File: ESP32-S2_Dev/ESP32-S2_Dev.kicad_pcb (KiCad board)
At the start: 4 copper layers, 47 x 67.3 mm, 114 parts, among them Q1 MMBT3906, Q2 BCW66GLT1G, Q3 BCW66GLT1G, U1 CP2102N-A01-GQFN28, U2 BD00C0AWFPS-ME2, U3 ESP32-S2, Y1 KC2520C40.0000C2YE00, Y2 Crystal

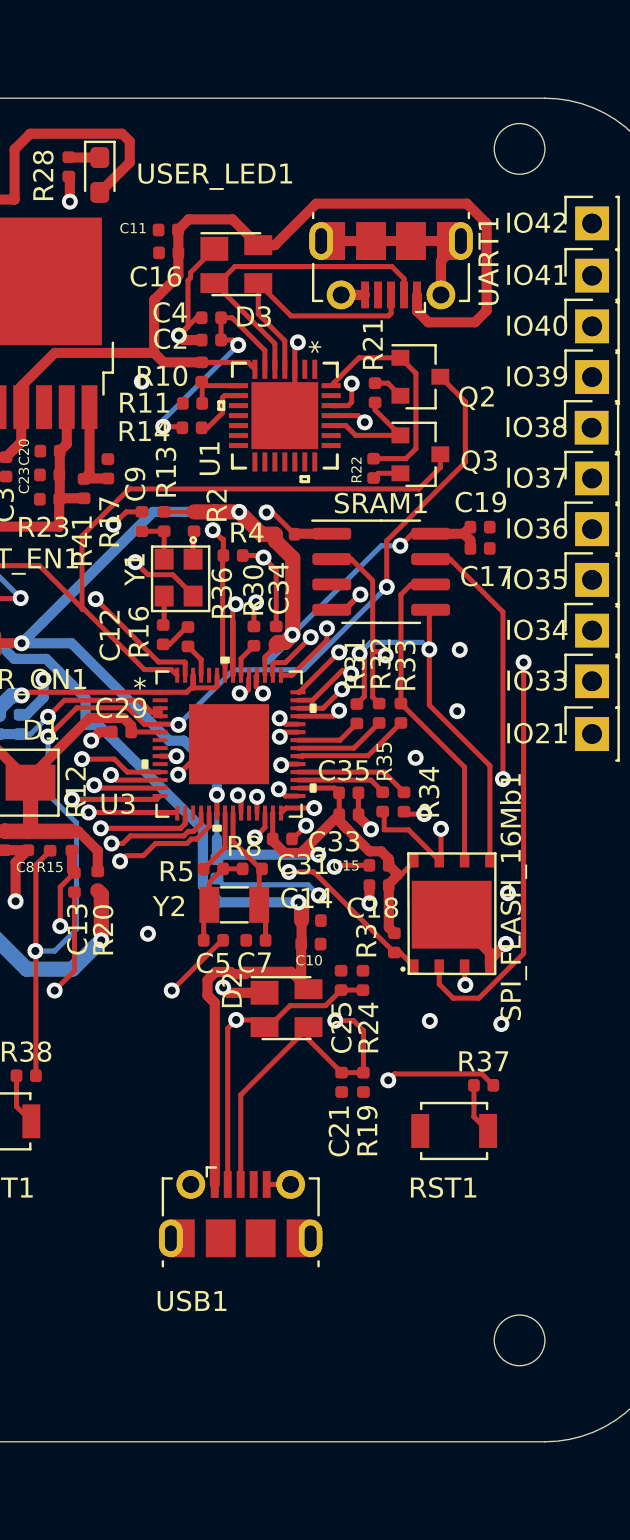
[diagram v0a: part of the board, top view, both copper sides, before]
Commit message: updated layout to move usb connectors closer to the edges, as they are today pluggin in will be nigh impossible.
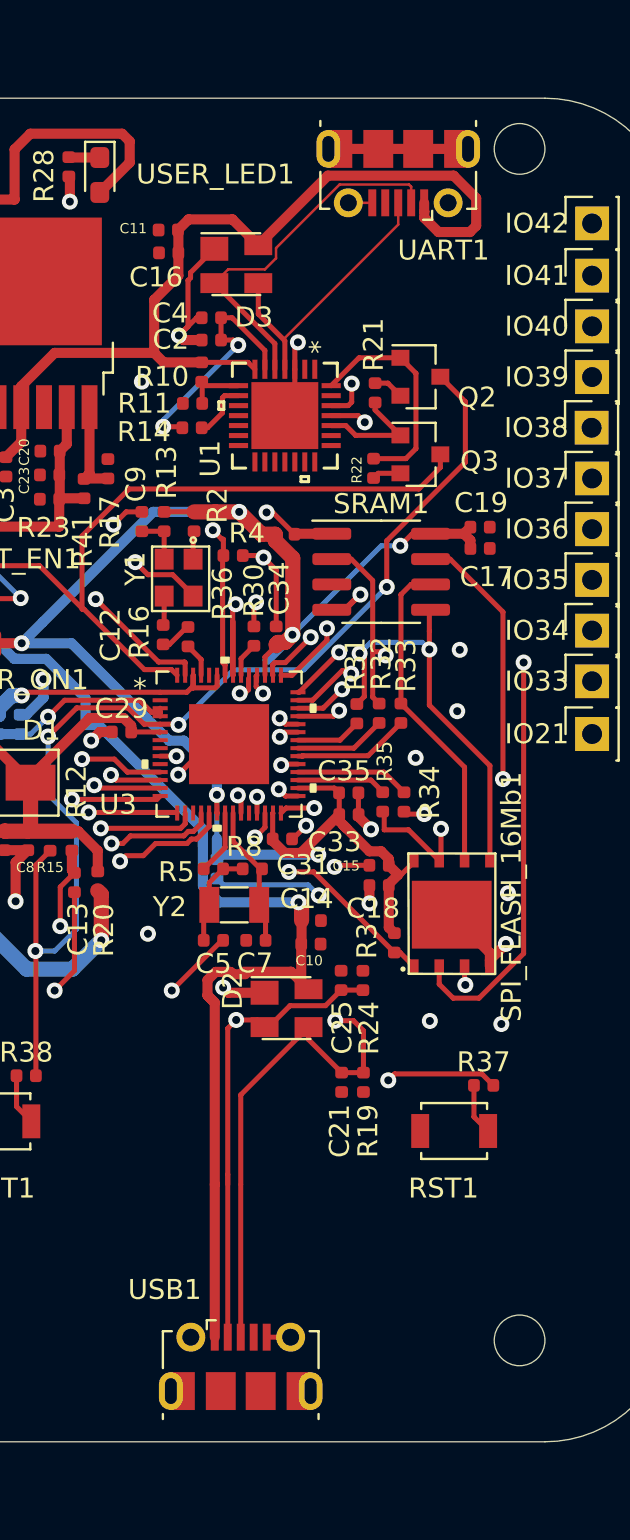
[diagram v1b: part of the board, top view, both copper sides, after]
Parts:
- moved USB1 7.65 mm to (121.9, 132.1)
- moved UART1 4.63 mm to (129.8, 72.4)
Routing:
- net /USB_DM: track 28.1 -> 36.3 mm
- net /USB_DP: track 29.4 -> 37.0 mm
- net /USB_5P0: track 110.3 -> 114.1 mm
- net GND: track 87.9 -> 84.8 mm
- net /USB_DMinus: track 16.5 -> 18.6 mm
- net /USB_DPlus: track 13.2 -> 14.1 mm

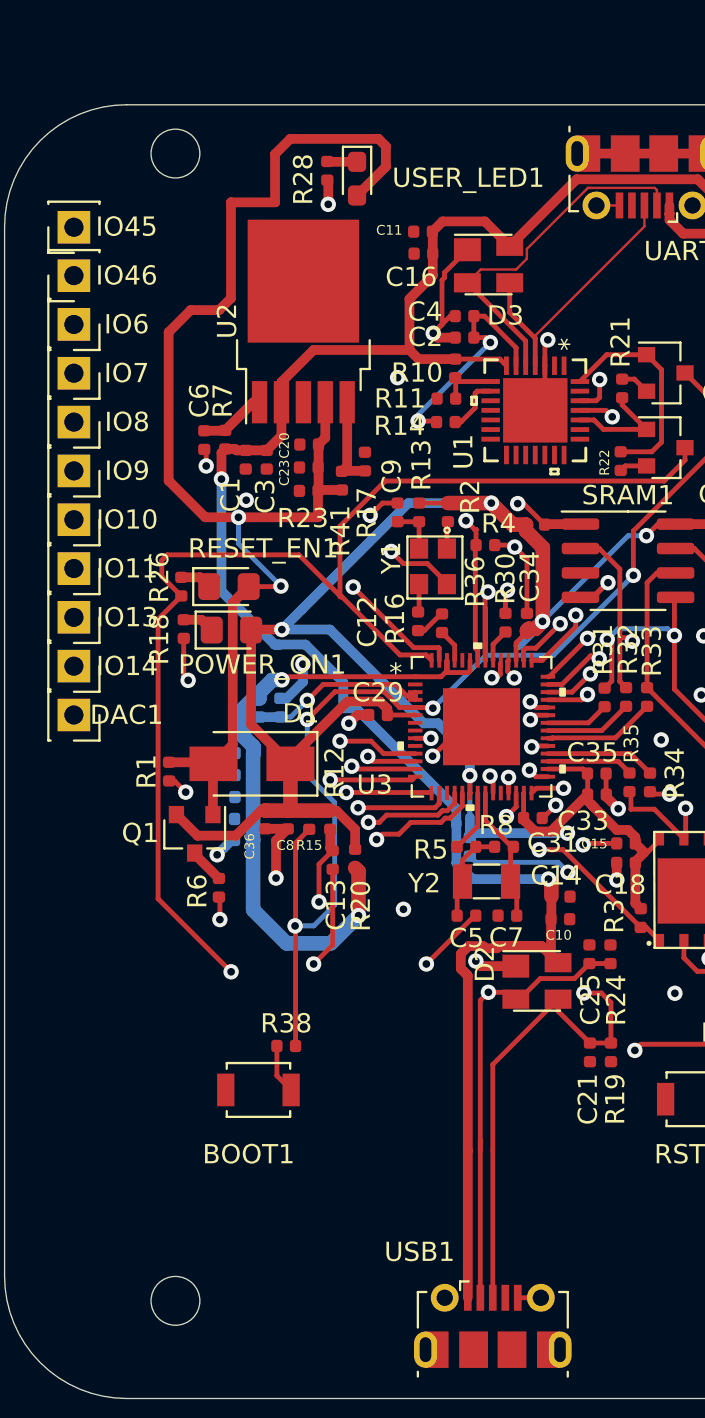
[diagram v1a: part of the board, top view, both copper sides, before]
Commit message: fixed the oscillator footprint mirror issue, made Q1 a SOT416, and added power input diodes
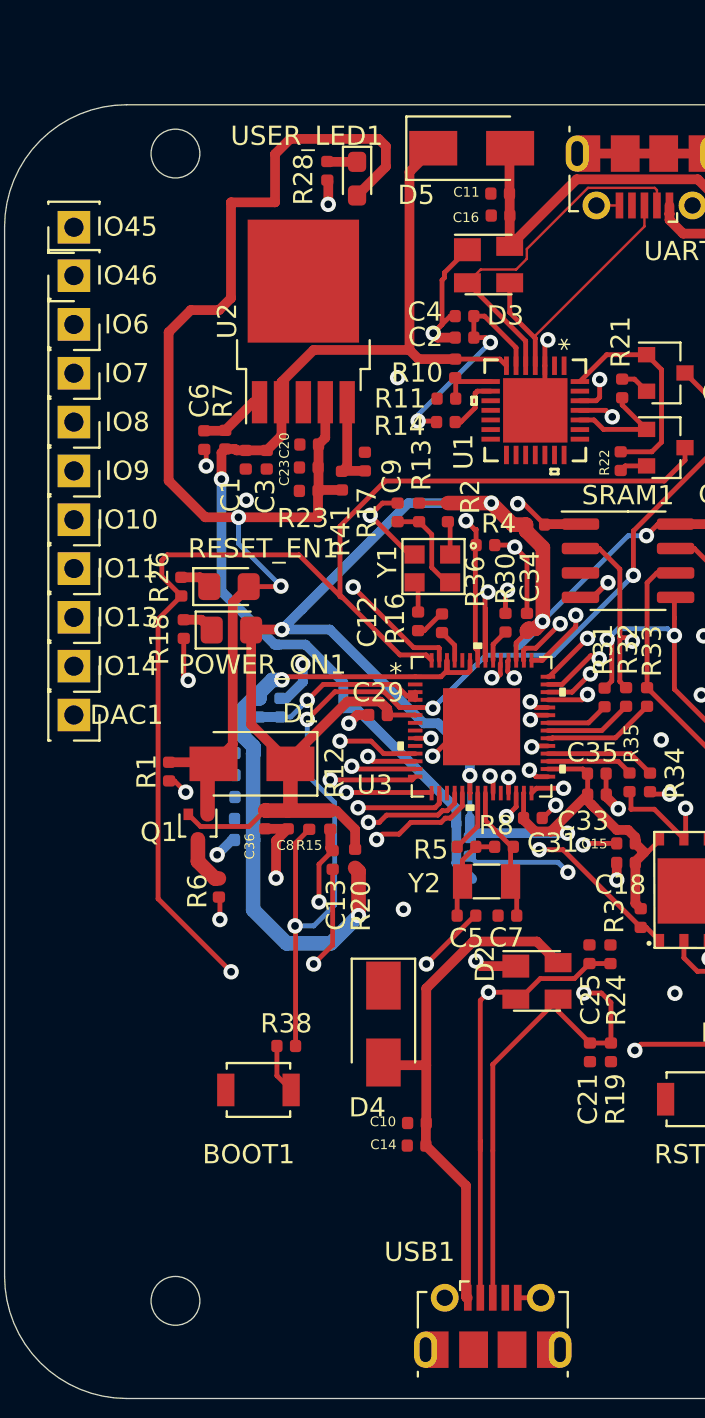
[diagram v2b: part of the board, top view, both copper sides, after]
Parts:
- added D4: B120-E3, Diode_SMD:D_SMA, F.Cu at (116.2, 116.4)
- added D5: B120-E3, Diode_SMD:D_SMA, F.Cu at (120.8, 70.8)
- Q1: footprint Package_TO_SOT_SMD:SOT-23 -> Package_TO_SOT_SMD:SOT-416
- moved C14 15.0 mm to (118.0, 122.7), turned to 0 degrees
- moved C10 13.0 mm to (118.0, 121.6), turned to 0 degrees
- moved C11 4.48 mm to (122.3, 73.2)
- moved C16 4.48 mm to (122.3, 74.3)
- moved Y1 2.04 mm to (118.8, 94.1), turned to 180 degrees
- moved Q1 0.40 mm to (106.6, 106.1)
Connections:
- C10 pad 2: /USB_5P0 -> Net-(C10-Pad2)
- C11 pad 2: /USB_5P0 -> Net-(C11-Pad2)
- C14 pad 2: /USB_5P0 -> Net-(C10-Pad2)
- C16 pad 2: /USB_5P0 -> Net-(C11-Pad2)
- D2 pad 4: /USB_5P0 -> Net-(C10-Pad2)
- D3 pad 4: /USB_5P0 -> Net-(C11-Pad2)
- UART1 pad 1: /USB_5P0 -> Net-(C11-Pad2)
- USB1 pad 1: /USB_5P0 -> Net-(C10-Pad2)
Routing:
- net /USB_5P0: track 114.1 -> 59.4 mm, vias 2 -> 1
- net Net-(C10-Pad2): track 0.00 -> 27.6 mm
- net Net-(C11-Pad2): track 0.00 -> 23.1 mm
- net /MCU_3P3_R: track 2.52 -> 5.10 mm
- net /MCU_3P3: track 117.0 -> 116.0 mm
- net Net-(Q1-Pad3): track 1.84 -> 2.61 mm
- net GND: track 84.8 -> 84.4 mm, vias 33 -> 32

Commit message: connected a net on the back for power
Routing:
- net /USB_5P0: track 59.4 -> 66.2 mm, vias 1 -> 2
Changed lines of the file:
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@@
     (thickness 1.6002)
     (drawings 19)
-    (tracks 881)
+    (tracks 885)
     (zones 0)
     (modules 116)
@@
       (padsonsilk false)
       (subtractmaskfromsilk false)
-      (outputformat 4)
+      (outputformat 1)
       (mirror false)
       (drillshape 0)
       (scaleselection 1)
-      (outputdirectory "../Outputs/V1/ESP32-S2_pdf/"))
+      (outputdirectory "../Outputs/V2/GERBER/"))
   )
   (net 0 "")
@@
   (segment (start 119.9642 81.8134) (end 118.0592 81.8134) (width 0.508) (layer Front) (net 2))
   (segment (start 112.597997 81.338601) (end 117.584401 81.338601) (width 0.508) (layer Front) (net 2))
-  (segment (start 120.850172 108.8644) (end 120.02519 108.039418) (width 0.508) (layer Back) (net 2))
   (segment (start 120.02519 106.06021) (end 120.02519 105.861028) (width 0.508) (layer Back) (net 2))
-  (segment (start 120.02519 108.039418) (end 120.02519 106.06021) (width 0.508) (layer Back) (net 2))
   (segment (start 110.830163 96.666001) (end 110.572319 96.666001) (width 0.508) (layer Back) (net 2))
   (segment (start 110.572319 96.666001) (end 107.803751 93.897433) (width 0.508) (layer Back) (net 2))
@@
   (segment (start 117.584401 72.077399) (end 117.584401 81.338601) (width 0.508) (layer Front) (net 2))
   (segment (start 118.8212 70.8406) (end 117.584401 72.077399) (width 0.508) (layer Front) (net 2))
+  (segment (start 116.2304 114.4082) (end 116.2304 112.8268) (width 0.508) (layer Front) (net 2))
+  (via (at 117.475 111.5822) (size 0.8) (drill 0.4) (layers Front Back) (net 2))
+  (segment (start 116.2304 112.8268) (end 117.475 111.5822) (width 0.508) (layer Front) (net 2))
+  (segment (start 120.02519 109.03201) (end 120.02519 107.75699) (width 0.508) (layer Back) (net 2))
+  (segment (start 117.475 111.5822) (end 120.02519 109.03201) (width 0.508) (layer Back) (net 2))
+  (segment (start 120.02519 107.75699) (end 120.02519 106.06021) (width 0.508) (layer Back) (net 2))
   (segment (start 131.11 74.256882) (end 131.1148 74.261682) (width 0.508) (layer Front) (net 102))
   (segment (start 131.11 73.82) (end 131.11 74.256882) (width 0.508) (layer Front) (net 102))

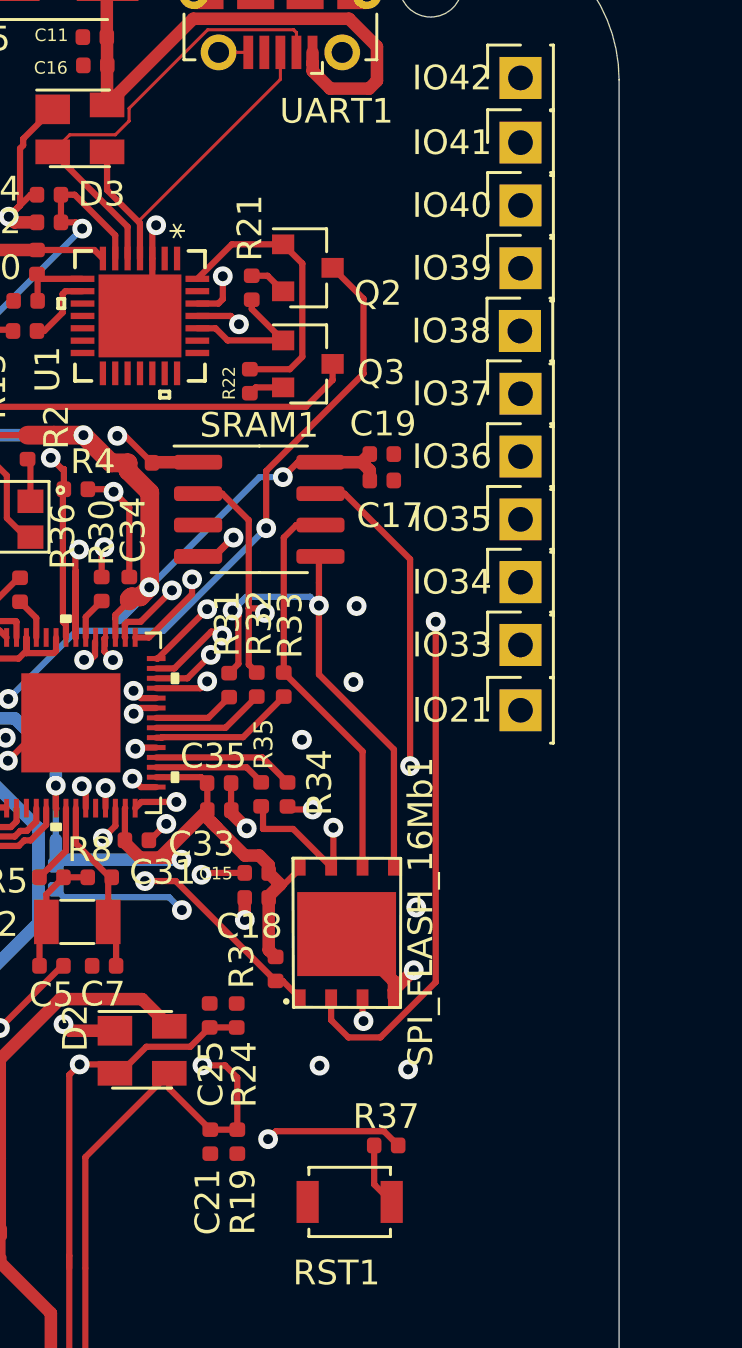
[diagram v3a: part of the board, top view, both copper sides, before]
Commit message: fixed RTS and DTR and added them as well as the reset timing capacitors to the layout
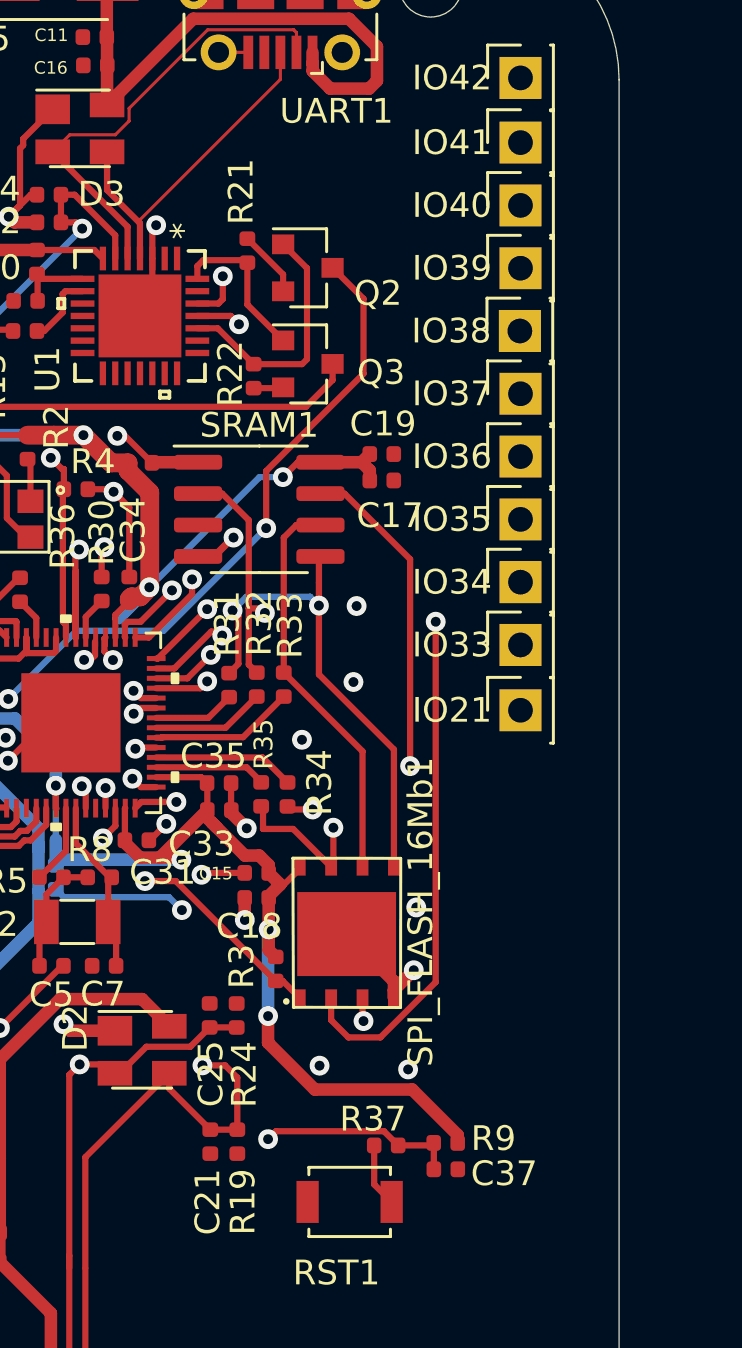
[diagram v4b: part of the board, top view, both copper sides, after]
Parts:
- added C37: 0.1u, Capacitor_SMD:C_0402_1005Metric, F.Cu at (136.5, 119.0)
- added R9: 10k, Resistor_SMD:R_0402_1005Metric, F.Cu at (136.5, 117.9)
- moved R21 1.51 mm to (128.5, 81.8)
- moved R22 0.26 mm to (128.7, 86.9)
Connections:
- Q2 pad 1: /DTR -> /RTS
- Q3 pad 1: /RTS -> /DTR
- R21 pad 2: /RTS -> /DTR
- R22 pad 2: /DTR -> /RTS
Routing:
- net /MCU_3P3: track 116.0 -> 130.2 mm, vias 6 -> 8
- net /DTR: track 11.2 -> 6.42 mm
- net /RTS: track 5.84 -> 10.2 mm
- net /RST_PROG: track 101.3 -> 103.9 mm
- net Net-(Q2-Pad2): track 1.53 -> 2.73 mm

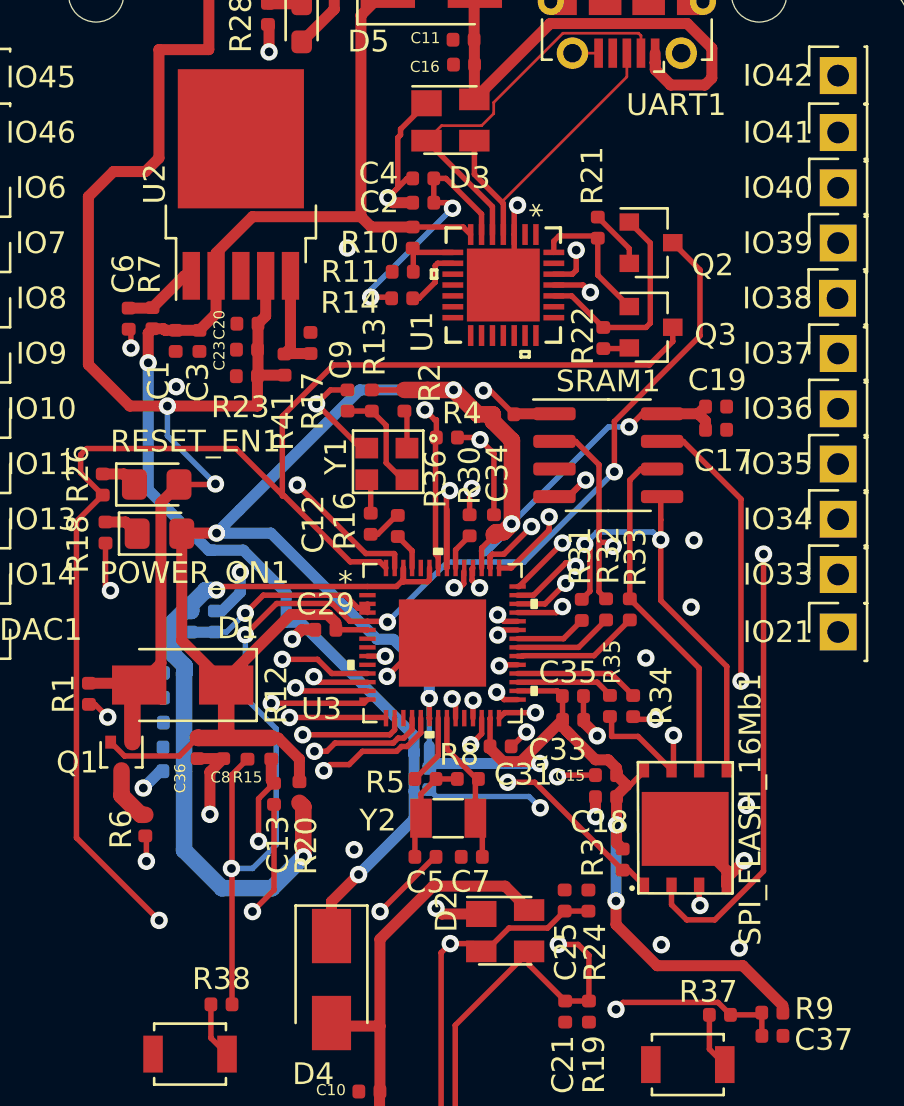
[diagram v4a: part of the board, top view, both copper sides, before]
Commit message: changed flash to gigadevice, since microchip is not supported
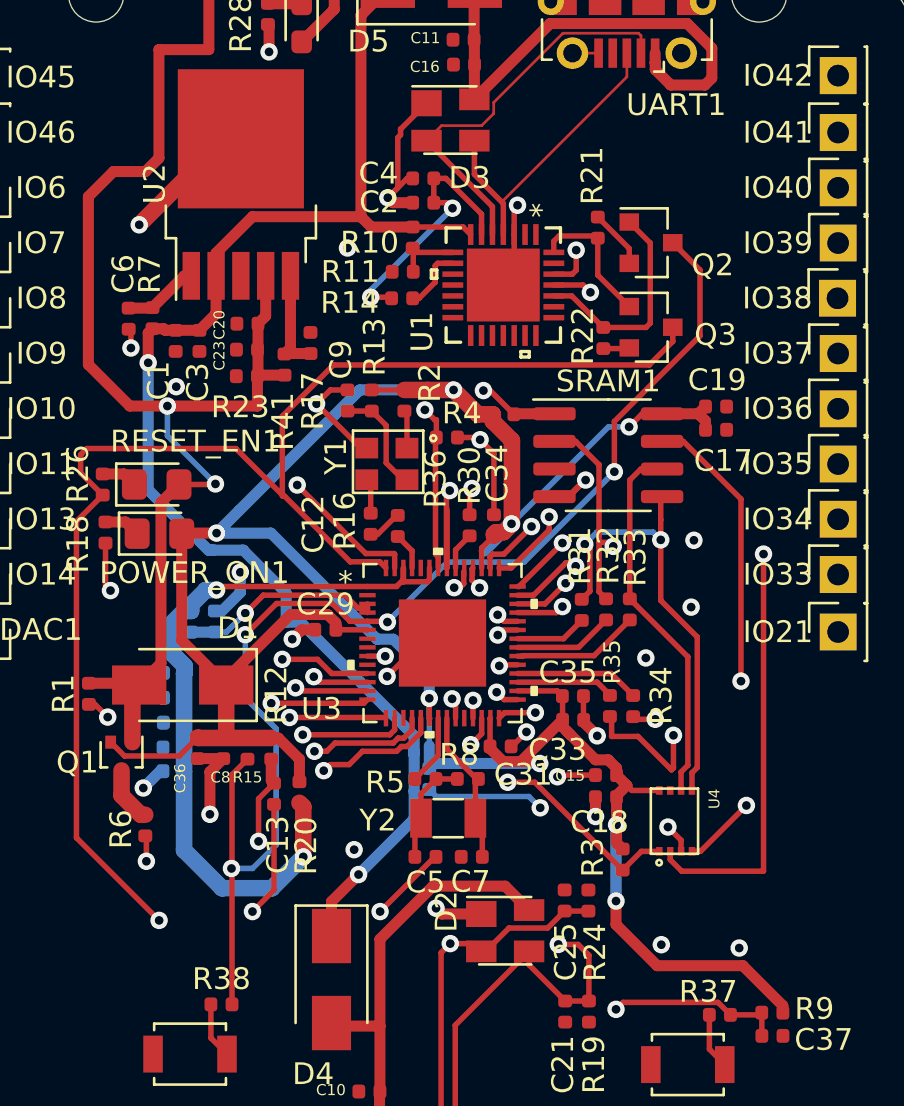
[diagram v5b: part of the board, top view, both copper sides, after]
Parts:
- removed SPI_FLASH_16Mb1: SST25VF016B-50-4I-QAF, Bub_flash:SST25VF016B-50-4I-QAF
- added U4: SPI_FLASH_8MEG, Bub_flash:USON8(2X3), F.Cu at (130.7, 109.2)
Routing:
- net GND: track 84.4 -> 89.2 mm
- net /SPIWP: track 11.4 -> 9.54 mm
- net /SPIQ: track 37.5 -> 36.0 mm
- net /SPICLK: track 16.3 -> 17.2 mm
- net /SPICS0: track 14.7 -> 15.5 mm
- net /MCU_3P3: track 130.2 -> 130.8 mm
